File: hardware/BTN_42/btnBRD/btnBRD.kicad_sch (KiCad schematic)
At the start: 117 parts, among them J1 Jack-DC, J10 Display Jumper, J2 MIDI-IN, J3 MIDI-OUT, J4 AudioJack2, J5 AudioJack2, J6 AudioJack2, J7 AudioJack2, J8 AudioJack2, J9 AudioJack2, SW1 1x1, SW10 3x2, SW11 4x2, SW12 5x2, SW13 6x2, SW14 7x2, SW15 1x3, SW16 2x3, SW17 3x3, SW18 4x3, SW19 5x3, SW2 2x1, SW20 6x3, SW21 7x3, SW22 1x4, SW23 2x4, SW24 3x4, SW25 4x4, SW26 5x4, SW27 6x4, SW28 7x4, SW29 1x5, SW3 3x1, SW30 2x5, SW31 3x5, SW32 4x5, SW33 5x5, SW34 6x5, SW35 7x5, SW36 1x6, SW37 2x6, SW38 3x6, SW39 4x6, SW4 4x1, SW40 5x6, SW41 6x6, SW42 7x6, SW43 cntrl1, SW44 cntrl2, SW45 cntrl3, SW46 cntrl4, SW47 cntrl5, SW48 cntrl6, SW5 5x1, SW6 6x1, SW7 7x1, SW8 1x2, SW9 2x2, U1 brain - teensy 4.0, U2 digital mux - 74hc4067m, U3 analog mux - 74hc4067m, U4 TXB0108DQSR, U5 6N138

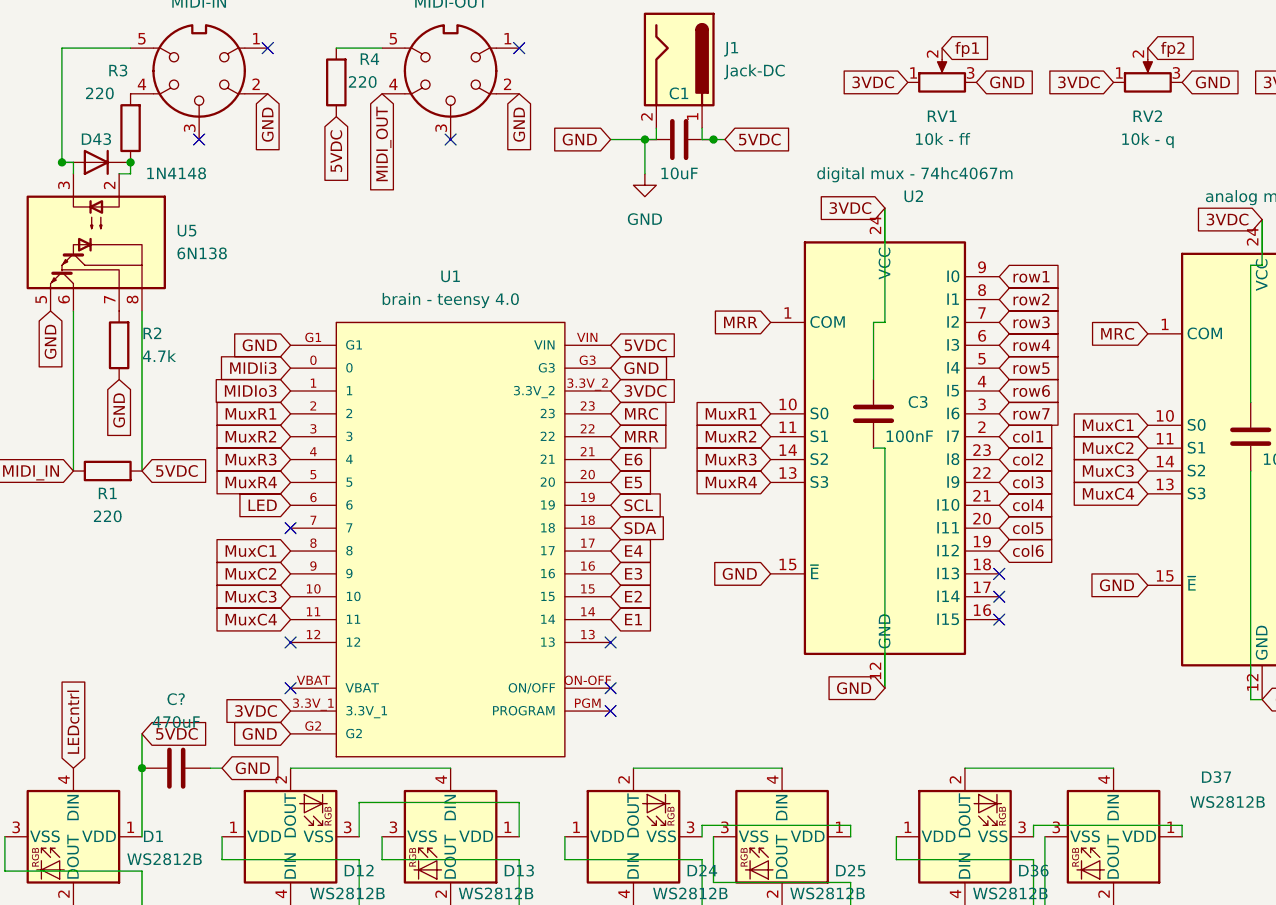
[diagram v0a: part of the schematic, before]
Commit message: resistors for pull up
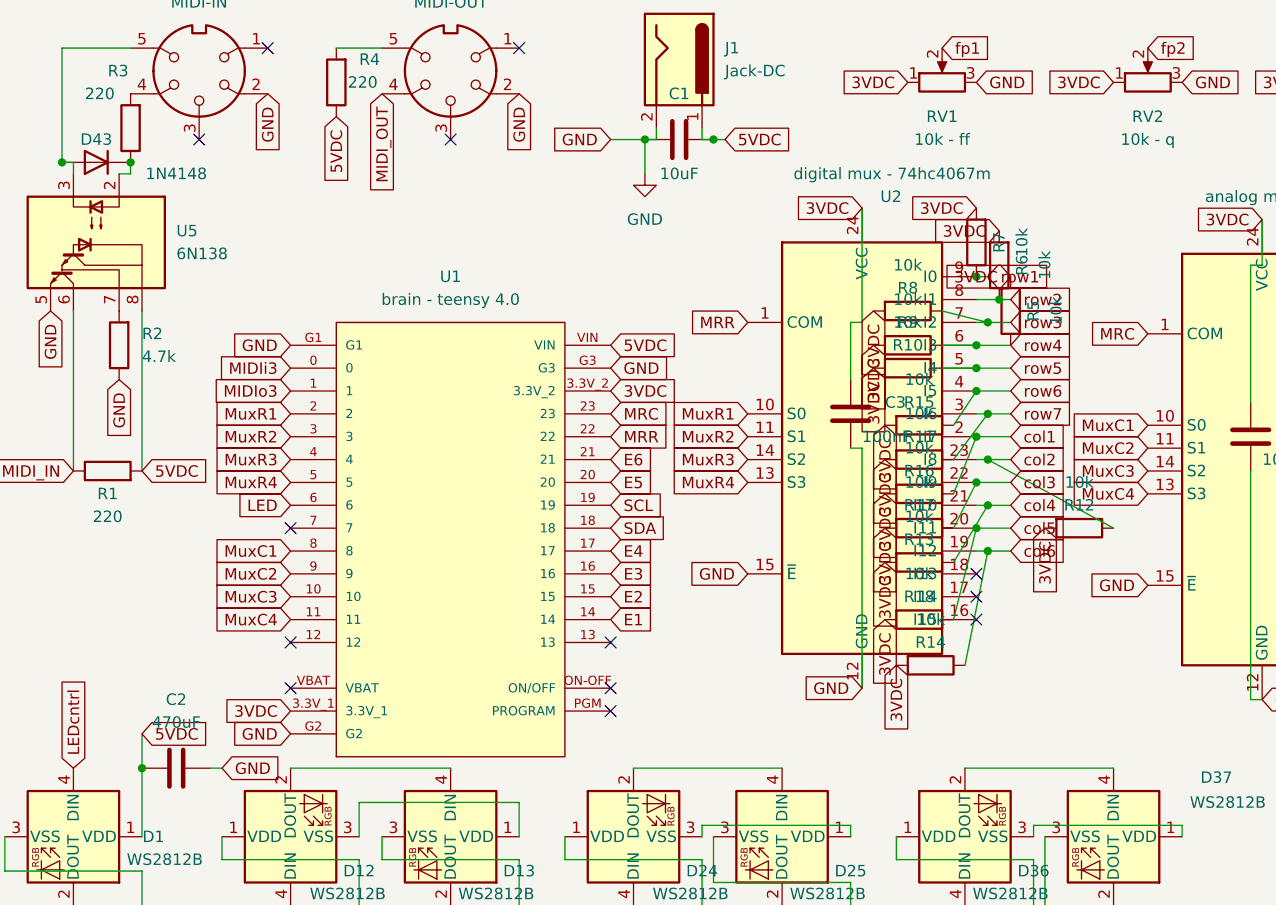
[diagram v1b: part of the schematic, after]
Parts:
- added R10, R11, R12, R13, R14, R15, R16, R17, R18, R5, R6, R7, R8, R9: 10k, Resistor_THT:R_Axial_DIN0204_L3.6mm_D1.6mm_P2.54mm_Vertical, symbol Device:R
- gave numbers to parts that had none: 1
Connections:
- net 3VDC: now also R10.2, R11.2, R12.2, R13.2, R14.2, R15.2, R16.2, R17.2, R18.2, R5.2, R6.2, R7.2, R8.2, R9.2
- net col1: now also R16.1
- net col2: now also R12.1
- net col3: now also R17.1
- net col4: now also R13.1
- net col5: now also R18.1
- net col6: now also R14.1
- net row1: now also R7.1
- net row2: now also R6.1
- net row3: now also R8.1
- net row4: now also R5.1, R9.1
- net row5: now also R10.1
- net row6: now also R15.1
- net row7: now also R11.1
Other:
- moved on the sheet: C3, U2
